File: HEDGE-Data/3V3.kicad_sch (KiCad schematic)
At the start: 16 parts, among them U2 A6986F

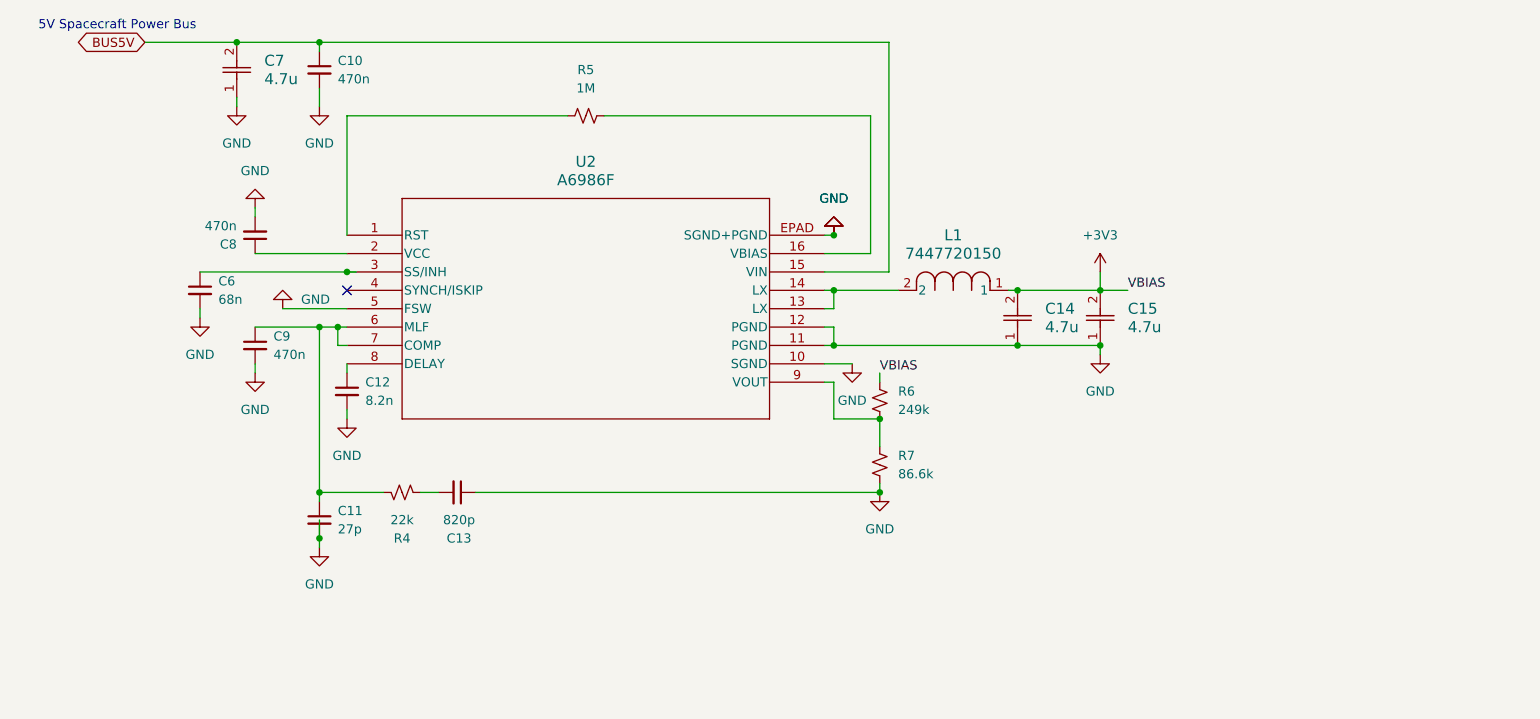
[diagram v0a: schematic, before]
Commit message: Refactor Data PCB files; enter RS485; enter Iridium radio power
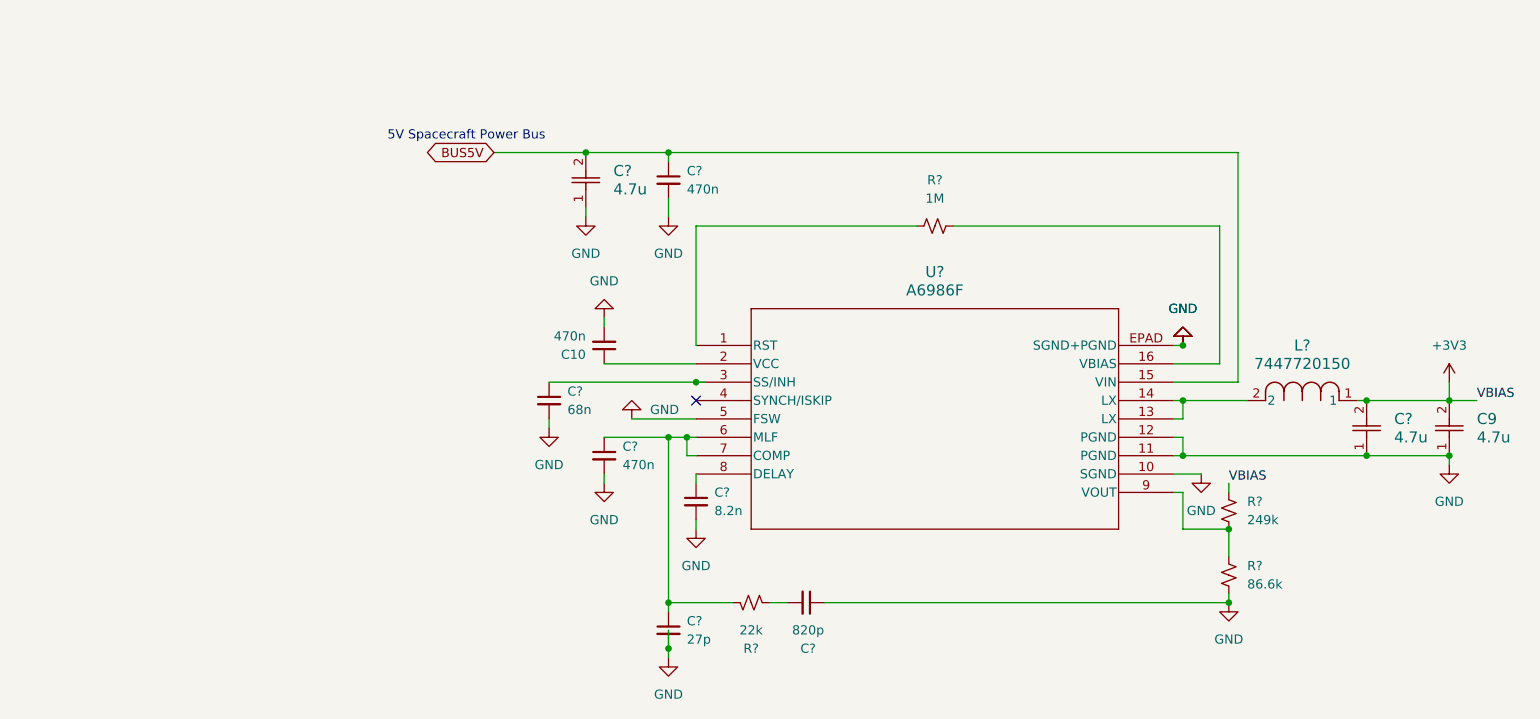
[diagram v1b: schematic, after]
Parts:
- removed C11: 27p, symbol Device:C_Small
- removed C12: 8.2n, symbol Device:C_Small
- removed C13: 820p, symbol Device:C_Small
- removed C14, C15: 4.7u, CAP_GRM15-5_MUR, symbol Cout:GRM155R60J475ME87D
- removed C6: 68n, symbol Device:C_Small
- removed C7: 4.7u, CAP_GRM21_MUR, symbol Cin:GRM219R61A475KE34D
- removed C8, C9: 470n, symbol Device:C_Small
- removed L1: 7447720150, IND_8095-WE-TI_8p3x10x5_WRE, symbol L1:7447720150
- removed R4: 22k, symbol Device:R_Small_US
- removed R5: 1M, symbol Device:R_Small_US
- removed R6: 249k, symbol Device:R_Small_US
- removed R7: 86.6k, symbol Device:R_Small_US
- removed U2: A6986F, HTSSOP_986F_STM, symbol A6986F:A6986F
- added C9, C?: 4.7u, CAP_GRM15-5_MUR, symbol Cout:GRM155R60J475ME87D
- added C? (x2): 470n, symbol Device:C_Small
- added C?: 27p, symbol Device:C_Small
- added C?: 820p, symbol Device:C_Small
- added C?: 8.2n, symbol Device:C_Small
- added C?: 68n, symbol Device:C_Small
- added C?: 4.7u, CAP_GRM21_MUR, symbol Cin:GRM219R61A475KE34D
- added L?: 7447720150, IND_8095-WE-TI_8p3x10x5_WRE, symbol L1:7447720150
- added R?: 86.6k, symbol Device:R_Small_US
- added R?: 249k, symbol Device:R_Small_US
- added R?: 22k, symbol Device:R_Small_US
- added R?: 1M, symbol Device:R_Small_US
- added U?: A6986F, HTSSOP_986F_STM, symbol A6986F:A6986F
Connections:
- net BUS5V: now also C?.1, C?.2, U?.15 (VIN); no longer C10.1
- net GND: now also C9.1, C?.1, C?.1, C?.1, C?.2, C?.2, C?.2, C?.2, C?.2, R?.2, U?.10 (SGND), U?.11 (PGND), U?.12 (PGND), U?.5 (FSW), U?.EPAD (SGND+PGND)
- net VBIAS: now also C9.2, C?.2, L?.1, R?.1
- new net: R?.1, R?.2, U?.9 (VOUT)
- new net: C?.1, C?.1, R?.1, U?.6 (MLF), U?.7 (COMP)
- new net: C?.2, R?.2
- new net: C?.1, U?.8 (DELAY)
- new net: C?.1, U?.3 (SS/INH)
- new net: R?.1, U?.1 (RST)
- new net: L?.2, U?.13 (LX), U?.14 (LX)
- new net: R?.2, U?.16 (VBIAS)
- new net: C10.1, U?.2 (VCC)
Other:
- company: Spacecraft Design Lab -> (none)
- title: HEDGE-Data PCB -> (none)
